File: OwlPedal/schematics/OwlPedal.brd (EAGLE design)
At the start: 103.1 x 79.5 mm, 86 parts, among them IC3 MC7805CDTG, IC6 TS974, J2 NEUTRIK_NMJ6HCD2, J3 NEUTRIK_NMJ6HCD2, J4 NEUTRIK_NMJ6HCD2, J5 NEUTRIK_NMJ6HCD2, J6 NEUTRIK_NMJ6HCD2, J7 NEUTRIK_NMJ6HCD2, J8 POWER_JACK, Q1 BS170, T1 2N3904

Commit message: routed
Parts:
- C17: device Rebel:153CLV-0405 -> Rebel:CPOL-5
- D1: value 1N4148DO35-10 -> 1N4148DO35-7; device diode:DO35-10 -> diode:DO35-7
- moved R24 34.2 mm to (12.7, 15.2)
- moved R23 29.9 mm to (12.7, 12.7)
- moved JP4 27.7 mm to (82.2, 51.8), turned to 90 degrees
- moved SW3 26.7 mm to (50.8, 58.4)
- moved R100 21.9 mm to (53.7, 38.1)
- moved C19 18.4 mm to (52.1, 30.5)
- moved R13 14.6 mm to (52.1, 27.9), turned to 180 degrees
- moved R2 12.7 mm to (86.4, 12.7)
- moved R1 12.0 mm to (86.4, 8.89)
- moved C16 8.63 mm to (41.9, 27.6), turned to 180 degrees
- moved R15 5.85 mm to (53.7, 35.2), turned to 180 degrees
- moved D4 5.68 mm to (44.2, 57.4)
- moved R26 5.58 mm to (41.9, 25.1)
- moved R20 5.24 mm to (67.3, 31.8)
- moved C13 4.46 mm to (28.3, 52.4), turned to 180 degrees
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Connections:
- net PE2 renamed A22
- net PE3 renamed A23
- net PE5 renamed A25
- removed net A3_PA3: JP7.1, R1.2, R23.2
- removed net A4_PA2: JP7.2, R2.2, R24.2
- removed net PE4: EXTSPI.2, Q1.D
- new net A24: EXTSPI.2
- new net A6: JP7.2, R2.2
- new net A7: JP7.1, R1.2
- net +3V3: now also J6.RN, J6.TN
- net A3_USART_TX: now also R24.2
- net A4_USART_RX: now also R23.2
- net A5: now also Q1.D
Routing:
- net +3V3: track 0.00 -> 165.6 mm
- net +5V: track 12.1 -> 133.1 mm, vias 1 -> 2
- net A21_ADC4: track 0.00 -> 103.7 mm, vias 0 -> 1
- net OUT_L: track 0.00 -> 85.4 mm, vias 0 -> 1
- net A20_ADC3: track 0.00 -> 71.9 mm, vias 0 -> 2
- net IN_L: track 0.00 -> 67.8 mm, vias 0 -> 2
- net OUT_R: track 0.00 -> 61.9 mm, vias 0 -> 2
- net A4_USART_RX: track 0.00 -> 55.5 mm, vias 0 -> 1
- net AOUT_A-: track 1.37 -> 53.4 mm, vias 1 -> 2
- net IN_R: track 0.00 -> 50.4 mm, vias 0 -> 2
- net A3_USART_TX: track 0.00 -> 49.4 mm, vias 0 -> 1
- net BYPASS: track 0.00 -> 47.5 mm
- net A19_ADC2: track 0.00 -> 46.4 mm, vias 0 -> 1
- net A16_SW3: track 0.00 -> 45.4 mm, vias 0 -> 1
- net DC_IN_L: track 9.72 -> 53.3 mm, vias 1 -> 2
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
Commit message: added bypass header
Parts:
- added JP6: (no value), SparkFun:1X02
- moved D1 3.18 mm to (74.3, 11.4)
- moved Q1 3.18 mm to (78.1, 14.0)
- moved T1 3.18 mm to (78.1, 7.62)
- moved C21 1.27 mm to (55.9, 53.3)
- moved C1 0.64 mm to (70.5, 30.2)
- moved R20 0.64 mm to (66.7, 31.8)
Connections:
- net +5V: now also JP6.1
- net A5: now also JP6.2
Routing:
- net +5V: track 133.1 -> 150.6 mm
- net BYPASS: track 47.5 -> 51.3 mm
- net A5: track 15.5 -> 19.2 mm
- net A4_USART_RX: track 55.5 -> 56.9 mm
- net A3_USART_TX: track 49.4 -> 50.7 mm
- net N$31: track 2.97 -> 4.24 mm
- net +3V3: track 165.6 -> 164.3 mm
- net A25: track 30.6 -> 29.8 mm
- net A18_ADC1: track 43.4 -> 42.7 mm
- net AIN_A: track 26.3 -> 25.6 mm
- net N$29: track 4.81 -> 4.22 mm
- net A21_ADC4: track 103.7 -> 103.1 mm
- net N$11: track 15.0 -> 15.5 mm
- net GND: vias 46 -> 66
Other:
- outline, holes or cut-outs redrawn

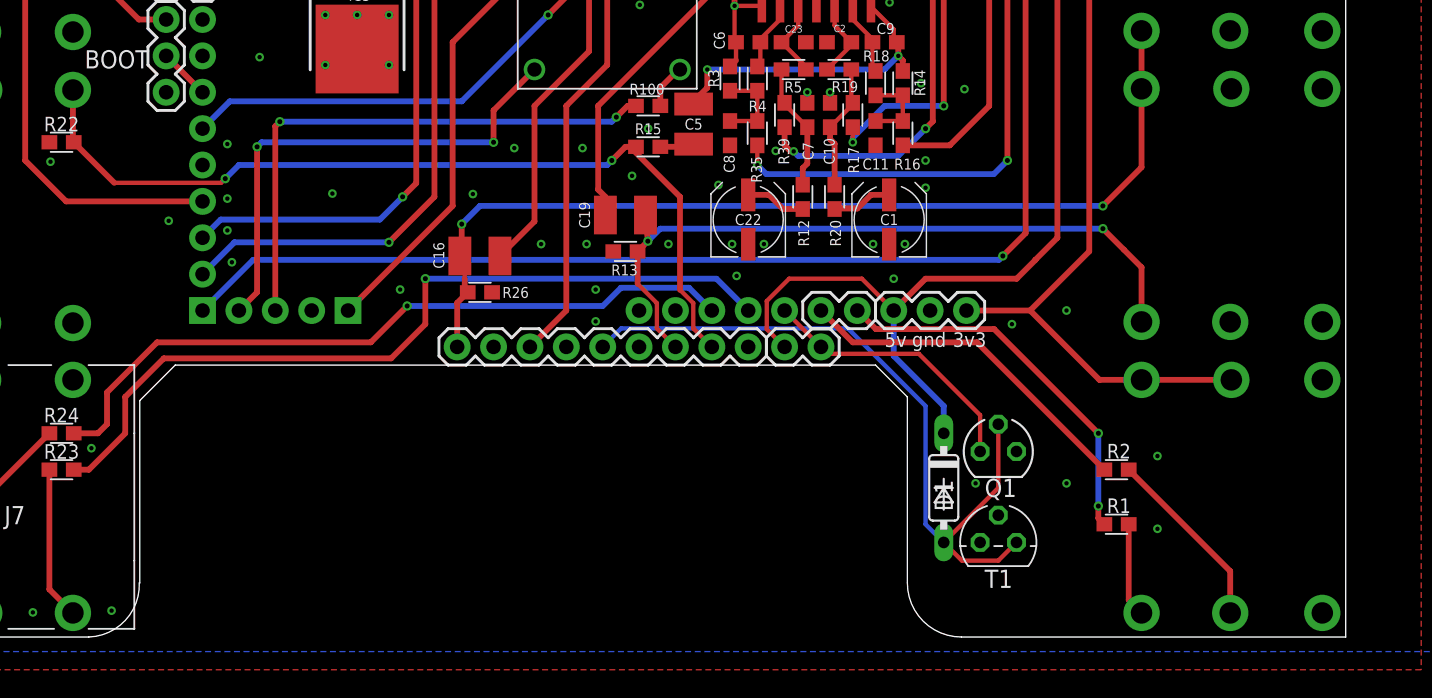
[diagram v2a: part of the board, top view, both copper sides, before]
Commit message: changed to smt bypass components
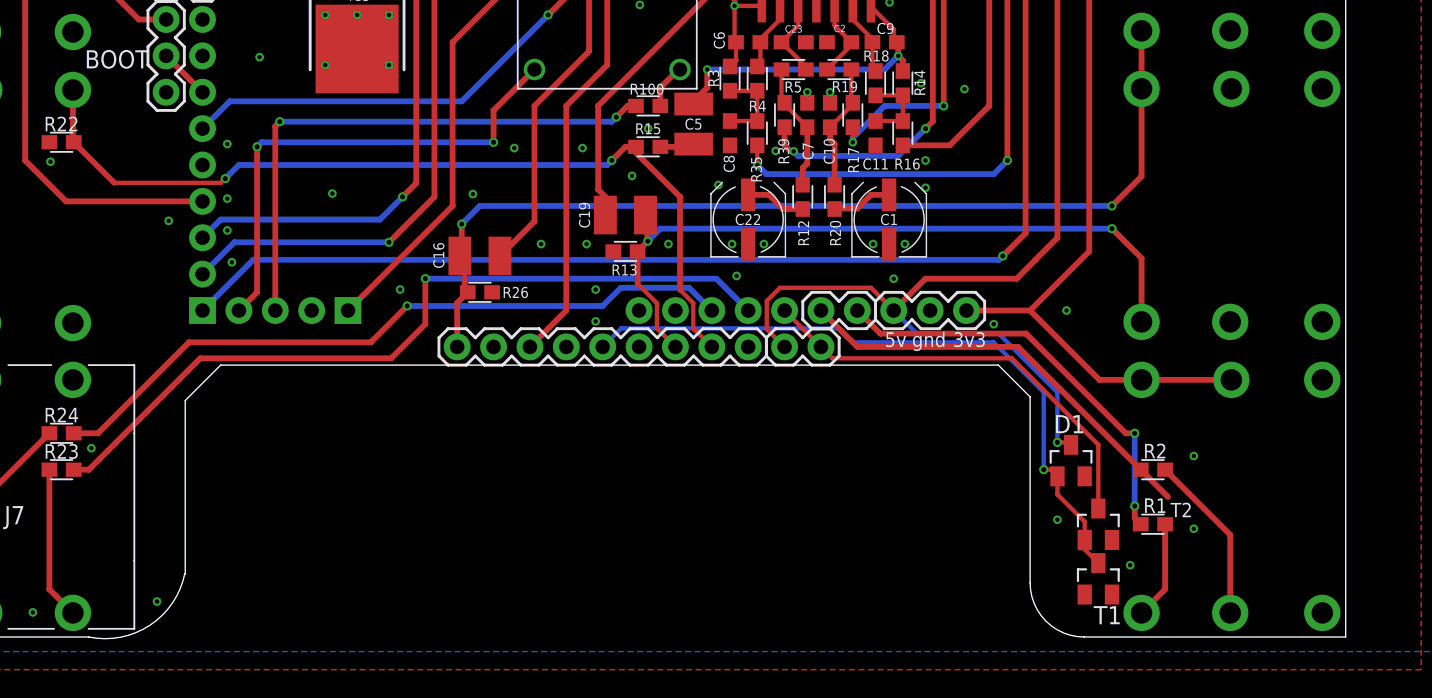
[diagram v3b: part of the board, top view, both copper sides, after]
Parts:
- removed Q1: BS170, transistor-small-signal:SOT54E
- added T2: 2N7002P, NXP_60_26022015:SOT23
- D1: value 1N4148DO35-7 -> BAS16; device diode:DO35-7 -> NXP_60_26022015:SOT23
- T1: value 2N3904 -> BC846; device transistor:TO92 -> NXP_60_26022015:SOT23
- moved D1 9.09 mm to (83.2, 13.3), turned to 0 degrees
- moved T1 7.43 mm to (85.1, 5.08)
- moved R1 2.54 mm to (88.9, 8.89)
- moved R2 2.54 mm to (88.9, 12.7)
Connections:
- net +5V: now also D1.3; no longer D1.C
- net A5: now also T2.3; no longer Q1.D
- net BYPASS: now also D1.1, T1.3, T2.1; no longer D1.A, Q1.G, T1.1
- net GND: now also T1.1, T2.2; no longer Q1.S, T1.2
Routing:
- net A5: track 19.2 -> 30.2 mm
- net +5V: track 150.6 -> 158.3 mm, vias 2 -> 3
- net A6: track 24.4 -> 29.6 mm
- net BYPASS: track 51.3 -> 47.0 mm, vias 0 -> 1
- net A7: track 26.9 -> 29.4 mm
- net A4_USART_RX: track 56.9 -> 55.4 mm
- net A3_USART_TX: track 50.7 -> 49.4 mm
- net N$12: track 12.9 -> 11.9 mm
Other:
- board size 103.1 x 79.5 mm -> 103.1 x 79.6 mm

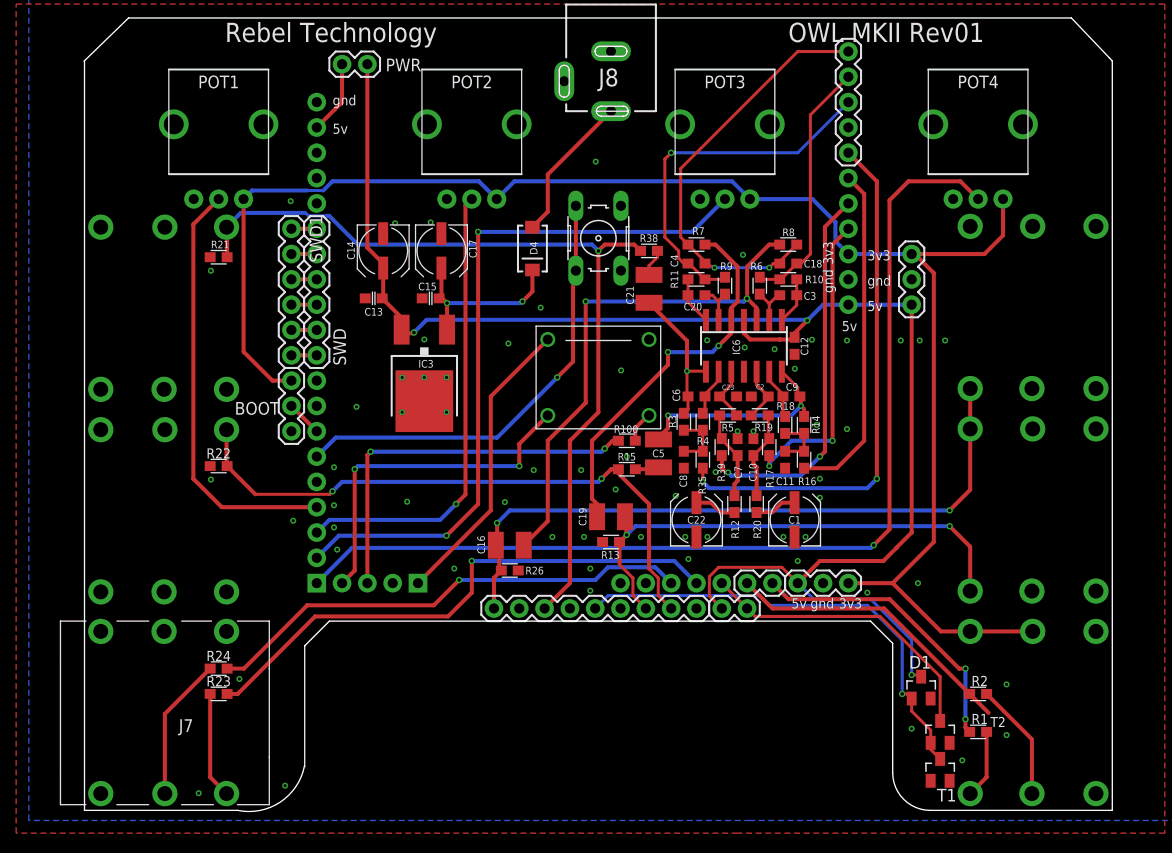
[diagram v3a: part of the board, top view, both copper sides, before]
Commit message: touched up placement and finalised routing
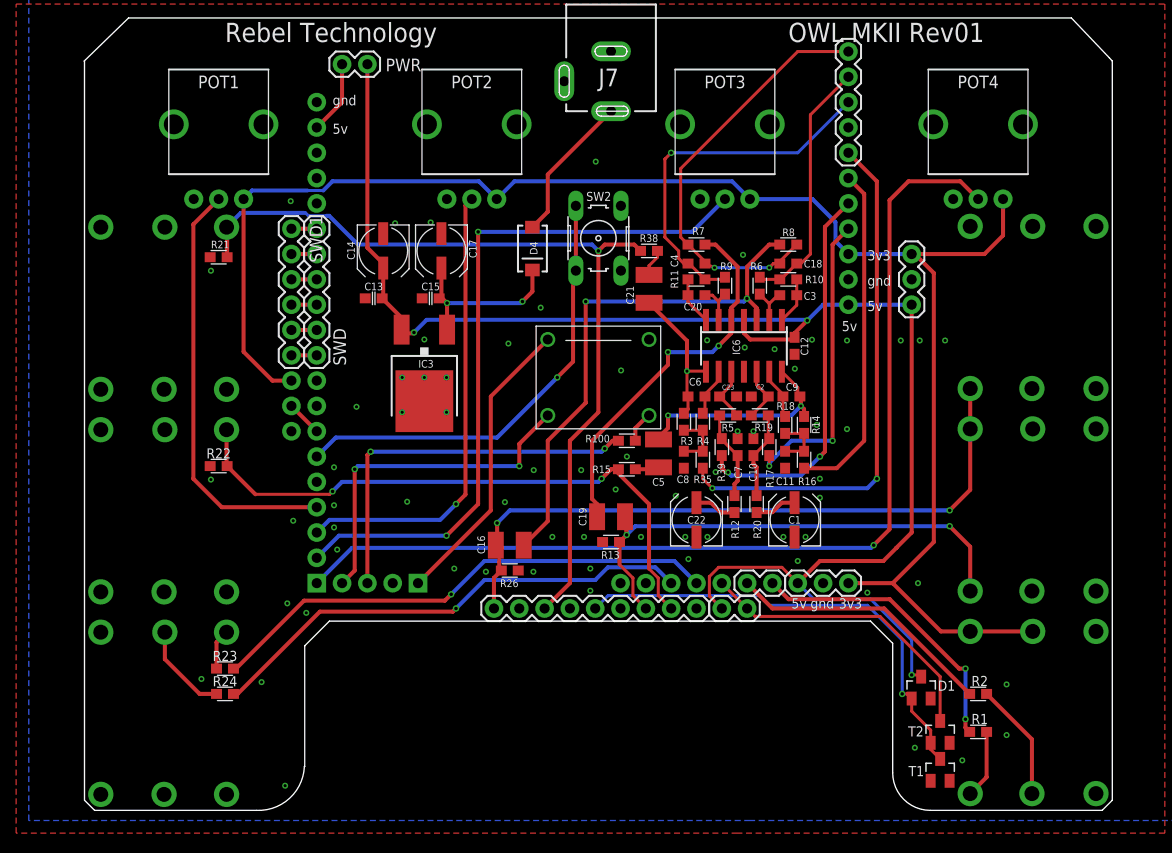
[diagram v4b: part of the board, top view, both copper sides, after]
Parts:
- removed J8: POWER_JACK, Rebel:DC_JACK_SLOT
- added J1: NEUTRIK_NMJ6HCD2, neutrik_jacks:NMJ6HCD2
- J7: value NEUTRIK_NMJ6HCD2 -> POWER_JACK; device neutrik_jacks:NMJ6HCD2 -> Rebel:DC_JACK_SLOT
- moved J3 90.0 mm to (94.6, 51.4), turned to 180 degrees
- moved J6 87.6 mm to (6.99, 10.8), turned to 0 degrees
- moved J7 84.2 mm to (52.1, 81.9)
- moved J2 20.3 mm to (6.99, 31.1)
- moved J4 20.3 mm to (94.6, 31.1)
- moved J5 20.3 mm to (94.6, 10.8)
- moved R23 2.62 mm to (13.3, 15.2)
- moved R24 2.62 mm to (13.3, 12.7)
- flipped BOOT to the bottom
- renumbered SW3 to SW2
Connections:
- net A16_SW3 renamed A16_SW2
- net A17_SW1 renamed A17
- net A1_LEDPWM2 renamed A1
- net A2_LEDPWM3 renamed A2
- net +3V3: now also J5.RN, J5.TN; no longer J6.RN, J6.TN
- net +9V: now also J7.PWR; no longer J8.PWR
- net GND: now also J1.S, J3.TN, J7.GND; no longer J4.TN, J7.S, J8.GND
- net IN_L: now also J3.T, J4.TN; no longer J4.T, J5.TN
- net IN_R: now also J4.T; no longer J5.T
- net N$12: now also J5.R; no longer J6.R
- net N$15: now also J5.T; no longer J6.T
- net N$2: now also J6.R; no longer J7.R
- net N$26: now also J6.T; no longer J7.T
- net OUT_L: now also J1.T; no longer J2.T
- net OUT_R: now also J2.T; no longer J3.T
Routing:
- net N$26: track 10.7 -> 4.07 mm
- net N$2: track 14.4 -> 9.33 mm
- net A4_USART_RX: track 55.4 -> 51.8 mm
- net A6: track 29.6 -> 26.9 mm
- net N$51: track 18.9 -> 18.0 mm
- net N$11: track 15.5 -> 14.8 mm
- net GND: vias 66 -> 70
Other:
- board size 103.1 x 79.6 mm -> 103.1 x 79.5 mm

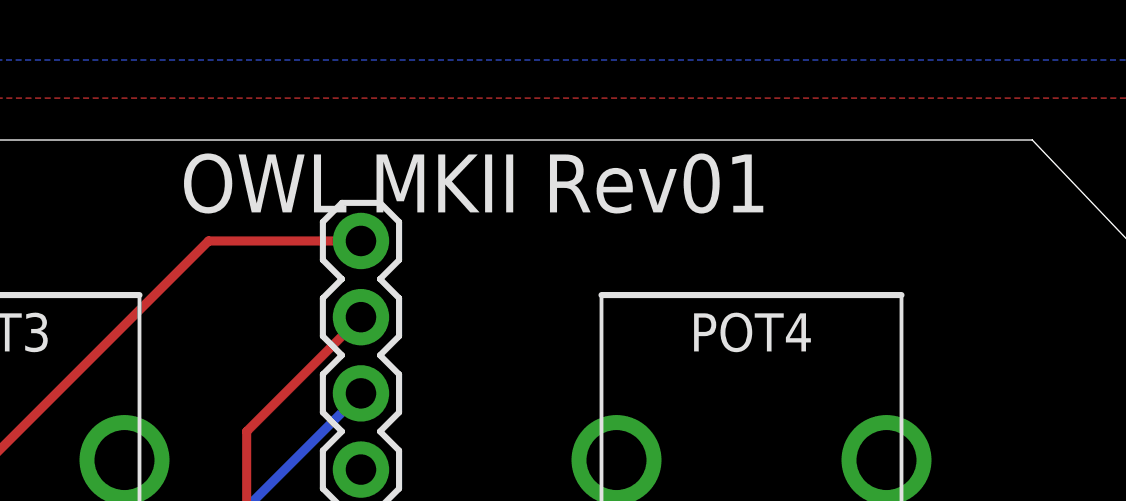
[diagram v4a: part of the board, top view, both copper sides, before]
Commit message: changed labels
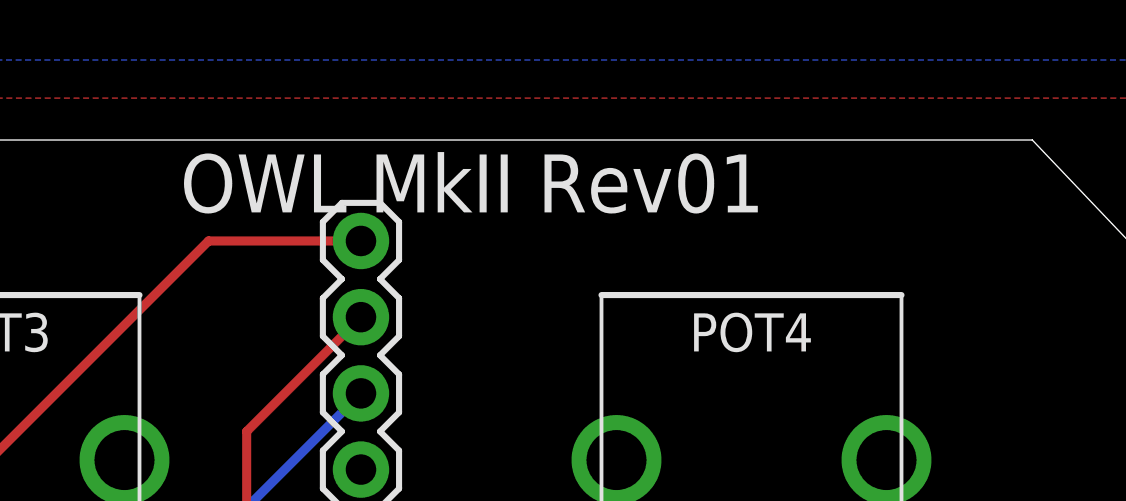
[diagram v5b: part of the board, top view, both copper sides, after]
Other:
- board text added: "OWL MkII Rev01"
- board text removed: "OWL MKII Rev01"
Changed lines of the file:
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@@
 <text x="80.645" y="54.9275" size="1.016" layer="22" font="vector" rot="SMR180" align="bottom-right">gnd</text>
 <text x="80.645" y="57.4675" size="1.016" layer="22" font="vector" rot="SMR180" align="bottom-right">3v3</text>
-<text x="69.85" y="78.105" size="1.9304" layer="21" font="vector">OWL MKII Rev01</text>
+<text x="69.85" y="78.105" size="1.9304" layer="21" font="vector">OWL MkII Rev01</text>
 <text x="13.335" y="78.105" size="1.9304" layer="21" font="vector">Rebel Technology</text>
 <text x="85.4075" y="78.105" size="1.9304" layer="22" font="vector" rot="MR0">Rebel Technology</text>
-<text x="36.5125" y="78.105" size="1.9304" layer="22" font="vector" rot="MR0">OWL MKII Rev01</text>
+<text x="36.5125" y="78.105" size="1.9304" layer="22" font="vector" rot="MR0">OWL MkII Rev01</text>
 <text x="18.415" y="40.64" size="1.27" layer="22" font="vector" rot="MR0">BOOT</text>
 <text x="75.185" y="49.0975" size="1.016" layer="22" font="vector" rot="SMR0" align="bottom-right">5v</text>
